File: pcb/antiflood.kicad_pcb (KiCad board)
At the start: 2 copper layers, 88 x 84 mm, 94 parts, among them J1 Barrel_Jack, J10 Screw_Terminal_01x02, J11 Screw_Terminal_01x02, J12 Screw_Terminal_01x02, J13 Screw_Terminal_01x02, J2 Conn_01x03_Male, J3 01x03, J4 01x03, J5 Conn_02x04_Odd_Even, J6 Conn_02x05_Odd_Even, J7 Conn_02x03_Odd_Even, J8 Screw_Terminal_01x02, J9 Screw_Terminal_01x02, K1 P-5, K2 P-5, Q1 2N3904, Q2 2N3904, SW1 SW_Push, SW2 SW_Push, SW3 SW_Push, U1 ATMEGA328P-AU, U2 TL7705, U3 LM1117-3.3, U4 MT3608, U5 MC34063, U6 TP4056, Y1 16MHz

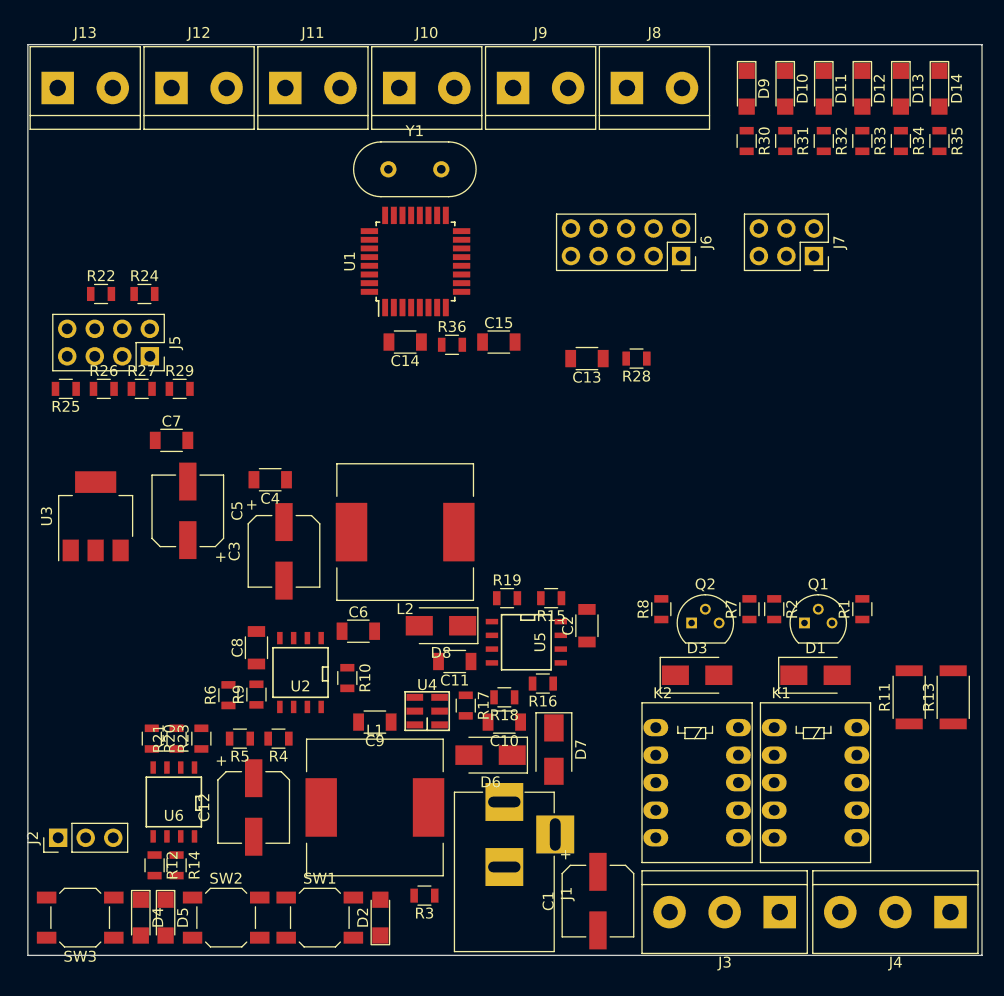
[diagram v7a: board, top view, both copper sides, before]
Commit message: PCB: alt placement
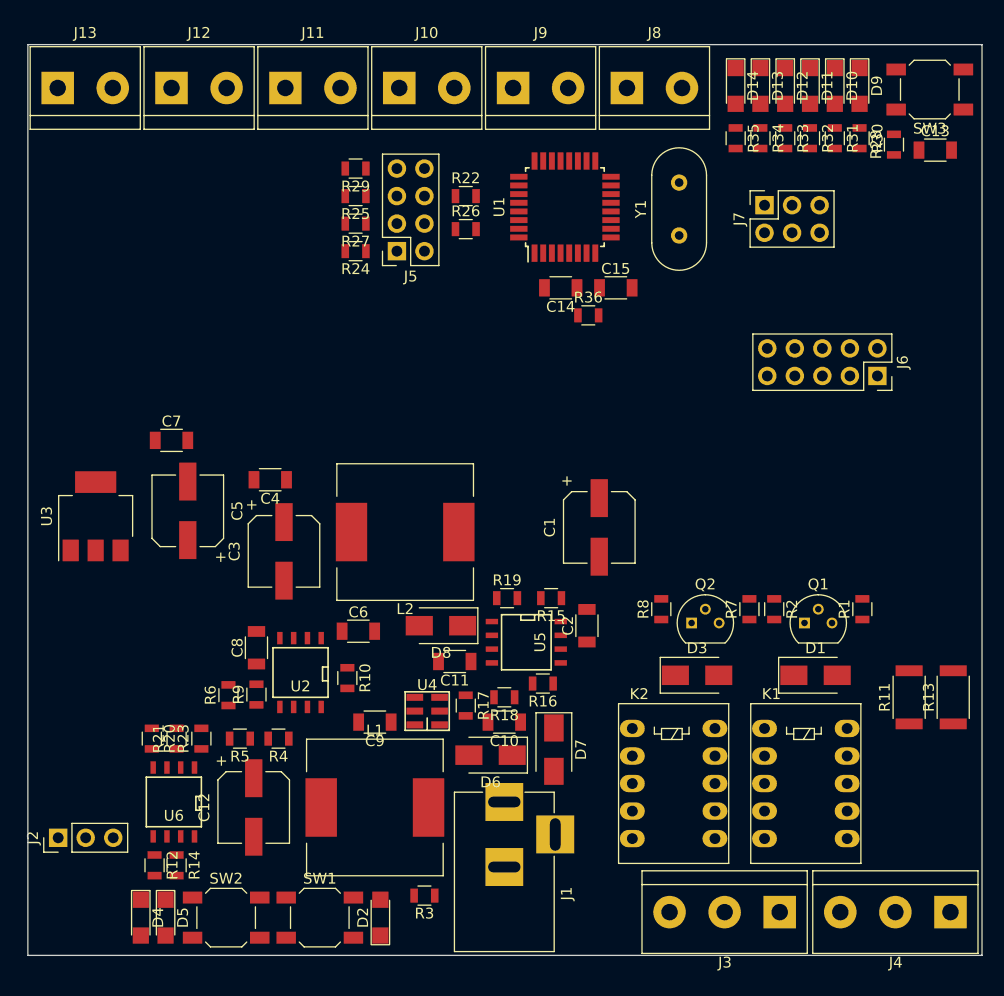
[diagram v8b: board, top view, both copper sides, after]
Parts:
- moved SW3 109.4 mm to (154.7, 55.1)
- moved C13 37.4 mm to (155.2, 60.7), turned to 0 degrees
- moved R26 36.5 mm to (111.9, 68.0)
- moved R22 34.8 mm to (111.9, 64.9)
- moved C1 34.5 mm to (124.2, 95.5)
- moved R25 32.1 mm to (101.7, 64.9)
- moved R28 30.9 mm to (151.4, 60.2), turned to 90 degrees
- moved Y1 27.5 mm to (131.6, 68.6), turned to 90 degrees
- moved R29 26.0 mm to (101.7, 62.4), turned to 180 degrees
- moved R27 24.9 mm to (101.7, 67.5), turned to 180 degrees
- moved J5 24.8 mm to (105.5, 70.0), turned to 180 degrees
- moved J6 21.2 mm to (149.9, 81.5)
- moved R24 19.9 mm to (101.7, 70.0), turned to 180 degrees
- moved D14 18.8 mm to (136.8, 54.8)
- moved R35 18.8 mm to (136.8, 59.6)
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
